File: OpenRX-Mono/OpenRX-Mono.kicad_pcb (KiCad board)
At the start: 6 copper layers, 9.6 x 13.6 mm, 47 parts, among them T1 0900PC16J0042001E, U1 ESP32-C3FH4, U2 TLV75533PDQNR, U3 TS2306A 240GF MSM 9_C2976675, U4 LR1121IMLTRT, U5 OW7EL89CENUYO3YLC-32M, U6 SKY13588-460LF, U7 RFX2401C, X1 CJ17-400001010B20

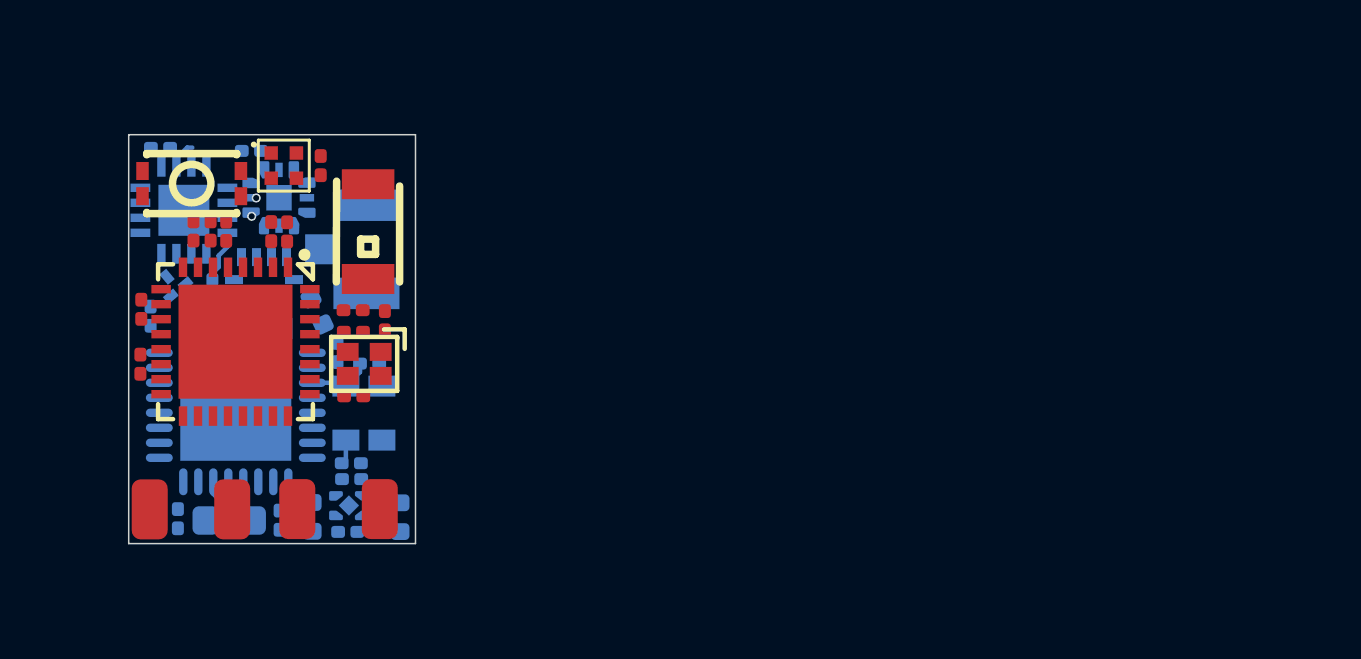
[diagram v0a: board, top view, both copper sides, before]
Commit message: Update schematics: Mono RF rewiring, SKY13414 port mapping, shared libs
Mono: disconnect IPD TX_LP (unused by ELRS), route TX_HP→RF3, RX→RF1,
RFX2401C ANT→RF4. Matches BetaFPV SuperX topology.

Co-Authored-By: Claude Opus 4.6 (1M context) <noreply@anthropic.com>
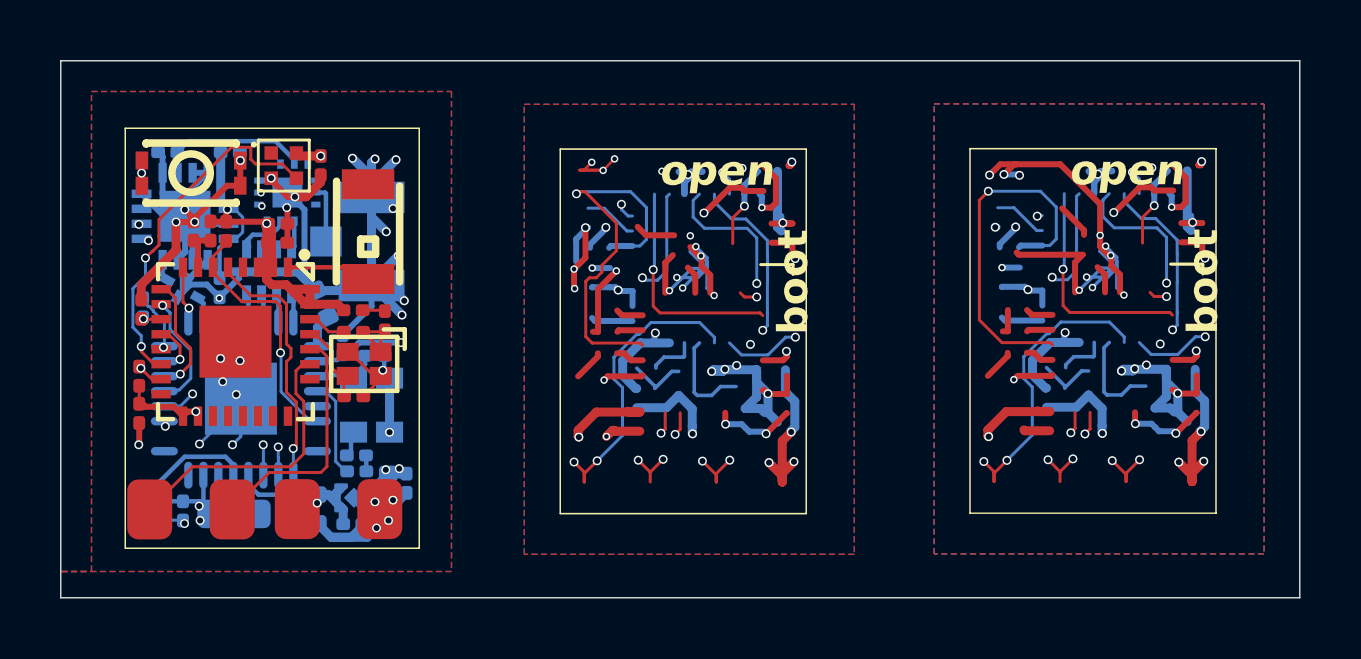
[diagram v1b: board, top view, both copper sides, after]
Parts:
- removed U6: SKY13588-460LF, OpenRX-Shared:QFN-12_L2.0-W2.0-P0.50-BL-EP0.8
- added U8: SKY13414-485LF, OpenRX-Shared:QFN-14_L2.0-W2.0-P0.45-BL-EP, B.Cu at (109.5, 85.4)
- C3: moved to F.Cu
- USB2: value DEA102700LT-6307A2 -> 2450FM07D0034
- moved C3 3.49 mm to (104.6, 92.7)
- moved C10 1.29 mm to (113.5, 95.1)
- moved C11 1.04 mm to (112.9, 95.2)
- moved C15 0.71 mm to (107.6, 84.0)
- moved C2 0.48 mm to (109.2, 87.0), turned to 0 degrees
- moved R3 0.40 mm to (104.6, 91.5), turned to 90 degrees
- moved R2 0.38 mm to (104.7, 89.2), turned to 90 degrees
- moved U5 0.37 mm to (112.3, 92.5)
- moved U3 0.35 mm to (106.3, 84.7)
- moved C1 0.34 mm to (109.2, 86.4), turned to 0 degrees
- moved C12 0.31 mm to (110.5, 95.9), turned to -90 degrees
- moved C13 0.31 mm to (111.8, 94.7)
- moved C20 0.31 mm to (110.7, 89.1)
- moved C21 0.31 mm to (111.4, 90.4)
- moved C22 0.31 mm to (109.4, 96.0)
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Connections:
- T1 pad 8: Net-(T1-RX) -> unconnected-(T1-TX_LP-Pad8)
- T1 pad 9: Net-(T1-RX) -> Net-(T1-TX_HP)
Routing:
- net (no net): track 0.00 -> 159.5 mm, vias 0 -> 26
- net GND: track 0.79 -> 157.1 mm, vias 0 -> 81
- net +3V3: track 1.75 -> 69.0 mm, vias 0 -> 27
- net +5V: track 0.00 -> 50.5 mm, vias 0 -> 10
- net Net-(U1-U0RXD): track 0.00 -> 30.7 mm, vias 0 -> 6
- net Net-(U1-U0TXD): track 0.00 -> 27.8 mm, vias 0 -> 4
- net /ESP32-C3 + LR1121 Mono/LED: track 0.00 -> 12.0 mm, vias 0 -> 2
- net /ESP32-C3 + LR1121 Mono/DIO8-1: track 0.17 -> 9.96 mm, vias 1 -> 2
- net /ESP32-C3 + LR1121 Mono/DIO7-1: track 0.13 -> 9.27 mm, vias 1 -> 2
- net /ESP32-C3 + LR1121 Mono/BUTTON: track 0.00 -> 8.89 mm, vias 0 -> 2
- net /ESP32-C3 + LR1121 Mono/TXEN: track 0.00 -> 8.59 mm, vias 0 -> 2
- net /ESP32-C3 + LR1121 Mono/IRQ1: track 0.00 -> 8.57 mm, vias 0 -> 1
- net /ESP32-C3 + LR1121 Mono/RST1: track 0.00 -> 8.42 mm, vias 0 -> 1
- net /ESP32-C3 + LR1121 Mono/RXEN: track 0.00 -> 7.71 mm, vias 0 -> 2
- net /ESP32-C3 + LR1121 Mono/MOSI: track 0.00 -> 4.03 mm, vias 0 -> 1
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- added copper zone on In3.Cu, net +3V3
- added copper zone on B.Cu, net GND
- added copper zone on F.Cu, net GND
- added copper zone on In1.Cu, net GND
- added copper zone on In2.Cu, net GND
- added copper zone on In3.Cu, net GND
- added copper zone on In4.Cu, net GND
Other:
- board size 9.6 x 13.6 mm -> 41.3 x 17.9 mm
- board text added: "5v"
- board text added: "GND"
- board text added: "RX"
- board text added: "TX"
- board text added: "boot"
- board text added: "open"
